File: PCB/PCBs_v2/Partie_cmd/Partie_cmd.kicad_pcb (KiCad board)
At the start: 2 copper layers, 51 parts, among them J2 Conn_01x04_Socket, J3 Conn_01x04_Socket, J4 Conn_01x11_Pin, J5 Conn_01x10_Pin, U1 ESP32-S3-DEVKITC-1-N8R2, U4 XL1509-5.0

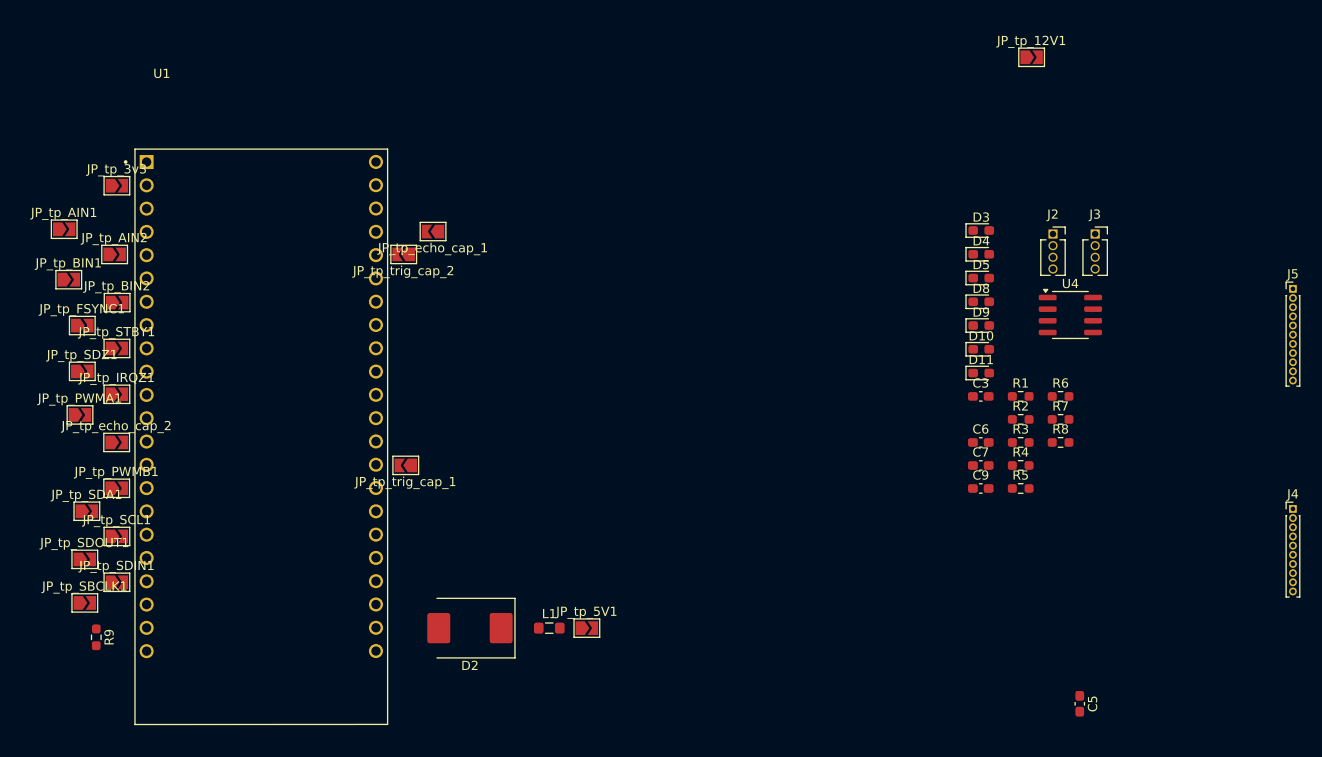
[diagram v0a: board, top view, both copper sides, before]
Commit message: Add new KiCad PCB and schematic files for Partie_cmd
Added new footprints, backup files, and autosave files for the Partie_cmd project in PCBs_v2, including ESP32 and SSOP5 footprints. Updated Partie_cmd.kicad_pcb, Partie_cmd.kicad_sch, and fp-lib-table to reflect new components and changes. Also added autosave and lock files for both PCB_v1 and PCBs_v2 projects.
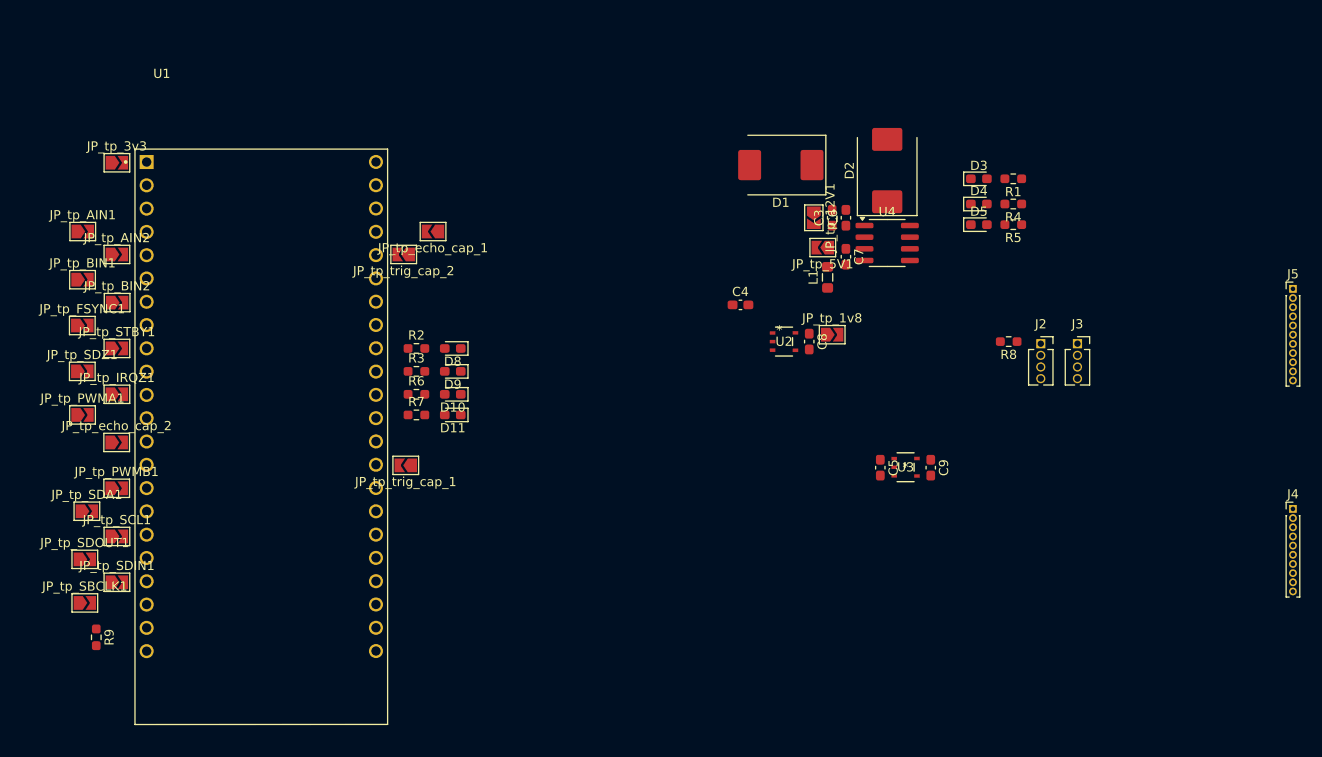
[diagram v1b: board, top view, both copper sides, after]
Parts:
- added C4: 1u, Capacitor_SMD:C_0603_1608Metric_Pad1.08x0.95mm_HandSolder, F.Cu at (127.8, 75.2)
- added C8: 1u, Capacitor_SMD:C_0603_1608Metric_Pad1.08x0.95mm_HandSolder, F.Cu at (135.2, 79.2)
- added D1: MBRS320, Diode_SMD:D_SMC, F.Cu at (132.2, 60.0)
- added JP_tp_1v8: SolderJumper_2_Open, Jumper:SolderJumper-2_P1.3mm_Open_TrianglePad1.0x1.5mm, F.Cu at (137.8, 78.5)
- added U2: BU18SD5WG-TL, footprints:SSOP5_ROM-L, F.Cu at (132.5, 79.2)
- added U3: BU33SD5WG-TR, footprints:SSOP5_ROM-L, F.Cu at (145.8, 93.0)
- moved R7 70.2 mm to (92.4, 87.2)
- moved R6 70.2 mm to (92.4, 85.0)
- moved D2 67.5 mm to (143.8, 60.6), turned to 90 degrees
- moved R3 66.4 mm to (92.4, 82.5)
- moved R2 66.4 mm to (92.4, 80.0)
- moved D8 57.9 mm to (96.4, 80.0), turned to 180 degrees
- moved D9 57.8 mm to (96.4, 82.5), turned to 180 degrees
- moved D10 57.8 mm to (96.4, 85.0), turned to 180 degrees
- moved D11 57.8 mm to (96.4, 87.2), turned to 180 degrees
- moved L1 48.8 mm to (137.2, 72.2), turned to 90 degrees
- moved JP_tp_5V1 48.8 mm to (136.7, 69.0), turned to 180 degrees
- moved C5 33.7 mm to (143.0, 93.0)
- moved JP_tp_12V1 29.5 mm to (135.8, 65.8), turned to -90 degrees
- moved R5 28.8 mm to (157.5, 66.5), turned to 180 degrees
- moved C6 28.6 mm to (139.2, 65.8), turned to 90 degrees
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
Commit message: fin schéma + Routage PCB cmd
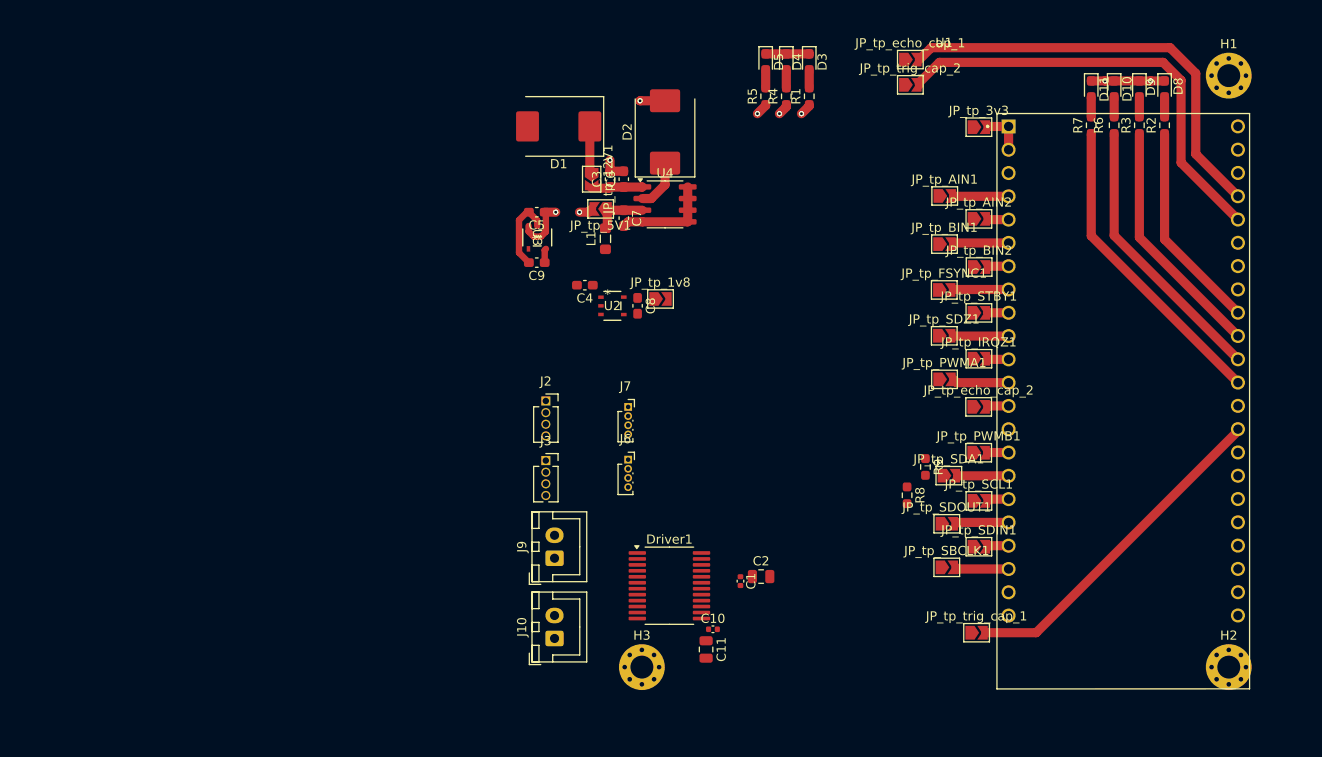
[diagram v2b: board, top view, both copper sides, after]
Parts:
- removed J4: Conn_01x11_Pin, Connector_PinHeader_1.00mm:PinHeader_1x10_P1.00mm_Vertical
- removed J5: Conn_01x10_Pin, Connector_PinHeader_1.00mm:PinHeader_1x11_P1.00mm_Vertical
- added C1: 0.1u, Capacitor_SMD:C_0402_1005Metric, F.Cu at (127.8, 105.4)
- added C10: 0.1u, Capacitor_SMD:C_0402_1005Metric, F.Cu at (124.8, 110.6)
- added C11: 10u, Capacitor_SMD:C_0805_2012Metric, F.Cu at (124.0, 112.8)
- added C2: 10u, Capacitor_SMD:C_0805_2012Metric, F.Cu at (130.0, 104.9)
- added Driver1: TB6612FNG, Package_SO:SSOP-24_5.3x8.2mm_P0.65mm, F.Cu at (120.0, 105.9)
- added H1: MountingHole_Pad, MountingHole:MountingHole_2.5mm_Pad_Via, F.Cu at (181.0, 50.2)
- added H2: MountingHole_Pad, MountingHole:MountingHole_2.5mm_Pad_Via, F.Cu at (181.0, 114.8)
- added H3: MountingHole_Pad, MountingHole:MountingHole_2.5mm_Pad_Via, F.Cu at (117.0, 114.8)
- added J10: Conn_01x02, Connector_JST:JST_XH_B2B-XH-A_1x02_P2.50mm_Vertical, F.Cu at (107.5, 111.6)
- added J6: Conn_01x04, Connector_PinSocket_1.00mm:PinSocket_1x04_P1.00mm_Vertical, F.Cu at (115.5, 92.1)
- added J7: Conn_01x04, Connector_PinSocket_1.00mm:PinSocket_1x04_P1.00mm_Vertical, F.Cu at (115.5, 86.4)
- added J9: Conn_01x02, Connector_JST:JST_XH_B2B-XH-A_1x02_P2.50mm_Vertical, F.Cu at (107.5, 102.9)
- moved JP_tp_3v3 94.1 mm to (153.8, 55.9)
- moved JP_tp_AIN1 94.1 mm to (150.0, 63.4)
- moved JP_tp_AIN2 94.1 mm to (153.8, 65.9)
- moved JP_tp_BIN1 94.1 mm to (150.0, 68.6)
- moved JP_tp_BIN2 94.1 mm to (153.8, 71.1)
- moved JP_tp_FSYNC1 94.1 mm to (150.0, 73.6)
- moved JP_tp_IRQZ1 94.1 mm to (153.8, 81.1)
- moved JP_tp_PWMA1 94.1 mm to (150.0, 83.4)
- moved JP_tp_PWMB1 94.1 mm to (153.7, 91.4)
- moved JP_tp_SBCLK1 94.1 mm to (150.2, 103.9)
- moved JP_tp_SCL1 94.1 mm to (153.8, 96.6)
- moved JP_tp_SDA1 94.1 mm to (150.5, 93.9)
- moved JP_tp_SDIN1 94.1 mm to (153.8, 101.6)
- moved JP_tp_SDOUT1 94.1 mm to (150.2, 99.1)
- moved JP_tp_SDZ1 94.1 mm to (150.0, 78.6)
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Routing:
- net Net-(JP_tp_trig_cap_2-B): track 0.00 -> 48.3 mm
- net Net-(JP_tp_echo_cap_1-B): track 0.00 -> 47.1 mm
- net GND: track 0.00 -> 37.6 mm, vias 0 -> 4
- net Net-(JP_tp_trig_cap_1-B): track 0.00 -> 36.8 mm
- net Net-(U1-GPIO36): track 0.00 -> 33.8 mm
- net Net-(U1-GPIO37): track 0.00 -> 30.2 mm
- net Net-(U1-GPIO38): track 0.00 -> 26.5 mm
- net Net-(U1-MTCK/GPIO39): track 0.00 -> 22.8 mm
- net 5V: track 0.00 -> 7.77 mm, vias 0 -> 2
- net 12V: track 0.00 -> 6.92 mm, vias 0 -> 1
- net Net-(JP_tp_PWMA1-B): track 0.00 -> 6.16 mm
- net 3.3V: track 0.00 -> 6.13 mm, vias 0 -> 1
- net Net-(JP_tp_5V1-A): track 0.00 -> 6.06 mm
- net Net-(JP_tp_BIN1-B): track 0.00 -> 6.06 mm
- net Net-(JP_tp_FSYNC1-B): track 0.00 -> 6.05 mm
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- added copper zone on In2.Cu, net GND
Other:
- copper layers 2 -> 4

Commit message: Routage pcb cmd
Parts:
- added D6: LED_Small, LED_SMD:LED_0603_1608Metric_Pad1.05x0.95mm_HandSolder, F.Cu at (130.4, 48.7)
- added H4: MountingHole_Pad, MountingHole:MountingHole_2.2mm_M2_DIN965_Pad, F.Cu at (116.8, 103.1)
- added H5: MountingHole_Pad, MountingHole:MountingHole_2.2mm_M2_DIN965_Pad, F.Cu at (132.5, 93.7)
- added J1: Barrel_Jack, Connector_BarrelJack:BarrelJack_Wuerth_694108106102_2.5x5.5mm, F.Cu at (113.2, 53.3)
- added J4: Conn_01x13_Pin, Connector_PinHeader_1.27mm:PinHeader_1x13_P1.27mm_Vertical, F.Cu at (131.1, 80.6)
- added JP1: Jumper_2_Bridged, TestPoint:TestPoint_2Pads_Pitch2.54mm_Drill0.8mm, F.Cu at (121.8, 49.8)
- added R10: 1.2k, Resistor_SMD:R_0603_1608Metric_Pad0.98x0.95mm_HandSolder, F.Cu at (130.4, 52.3)
- R4: value 120 -> 1.2k
- R5: value 82 -> 820
- moved JP_tp_3v3 40.7 mm to (117.9, 75.2), turned to -90 degrees
- moved JP_tp_5V1 19.2 mm to (130.3, 71.9), turned to -90 degrees
- moved D1 17.9 mm to (125.2, 60.2)
- moved C3 17.9 mm to (130.8, 65.9)
- moved C6 17.9 mm to (132.3, 65.9)
- moved C7 17.9 mm to (132.3, 70.2)
- moved D2 17.9 mm to (136.8, 60.8)
- moved JP_tp_12V1 17.9 mm to (128.8, 65.9)
- moved U4 17.9 mm to (136.8, 68.7)
- moved L1 16.6 mm to (129.5, 69.4), turned to 0 degrees
- moved C4 15.1 mm to (124.6, 67.0), turned to 90 degrees
- moved C10 14.0 mm to (138.7, 112.0)
- moved C11 14.0 mm to (138.0, 114.2)
- moved Driver1 14.0 mm to (134.0, 107.2)
- moved H3 14.0 mm to (131.0, 116.1)
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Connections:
- C1 pad 1: 5V -> 3.3V
- C2 pad 1: 5V -> 3.3V
- Driver1 pad 20: 5V -> 3.3V
- Driver1 pad 3: (no net) -> GND
- R4 pad 1: 3.3V -> 5V
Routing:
- net 12V: track 6.92 -> 184.8 mm, vias 1 -> 4
- net 5V: track 7.77 -> 168.9 mm, vias 2 -> 5
- net 3.3V: track 6.13 -> 118.0 mm, vias 1 -> 3
- net Echo_cap_1: track 0.00 -> 62.9 mm, vias 0 -> 1
- net Trig_cap_2: track 0.00 -> 61.1 mm
- net BIN2: track 0.00 -> 56.9 mm, vias 0 -> 4
- net SCL: track 0.00 -> 56.3 mm, vias 0 -> 5
- net SDA: track 0.00 -> 55.9 mm, vias 0 -> 4
- net BIN1: track 0.00 -> 51.2 mm, vias 0 -> 2
- net AIN1: track 0.00 -> 50.3 mm, vias 0 -> 2
- net AIN2: track 0.00 -> 49.1 mm, vias 0 -> 2
- net GND: track 37.6 -> 86.3 mm, vias 4 -> 14
- net Trig_cap_1: track 0.00 -> 43.6 mm, vias 0 -> 1
- net STBY: track 0.00 -> 41.0 mm, vias 0 -> 4
- net 1.8V: track 1.36 -> 41.7 mm, vias 1 -> 2
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- added copper zone on In1.Cu, net 1.8V
- added copper zone on In1.Cu, net 12V
- added copper zone on In1.Cu, net 3.3V
- added copper zone on In1.Cu, net 5V
- added copper zone on B.Cu, net GND
- added copper zone on F.Cu, net GND
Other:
- board outline added: 79.2 x 75 mm
- board text added: "G-Vidon S-Remy A-Djokic A-Taillepierre J-Lepetit C-Laroche"
- board text added: "NOMAD_"

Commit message: Fin routage pcb cmd
:(
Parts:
- removed J7: Conn_01x04, Connector_PinSocket_1.00mm:PinSocket_1x04_P1.00mm_Vertical
- J4: value Conn_01x13_Pin -> Conn_01x12; footprint Connector_PinHeader_1.27mm:PinHeader_1x13_P1.27mm_Vertical -> Connector_PinHeader_1.27mm:PinHeader_1x12_P1.27mm_Vertical
- moved J3 30.3 mm to (111.2, 61.8)
- moved J2 17.7 mm to (111.2, 68.3)
- moved J6 14.7 mm to (136.8, 82.2)
- moved H5 5.17 mm to (130.0, 98.2)
- moved H4 4.86 mm to (117.2, 98.2)
- moved J9 3.22 mm to (121.2, 107.5)
- moved J10 2.92 mm to (121.2, 115.9)
- moved J4 1.07 mm to (130.0, 80.8)
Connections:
- J4 pad 1: FSYNC -> SDZ
- J4 pad 11: 12V -> GND
- J4 pad 12: GND -> 12V
- J4 pad 2: SBCLK -> IRQZ
- J4 pad 3: SDIN -> 1.8V
- J4 pad 4: SCL -> SDA
- J4 pad 5: SDA -> SCL
- J4 pad 6: SDZ -> SBCLK
- J4 pad 7: IRQZ -> FSYNC
- J4 pad 8: SDOUT -> SDIN
- J4 pad 9: 1.8V -> SDOUT
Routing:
- net 5V: track 168.9 -> 233.8 mm, vias 5 -> 7
- net Trig_cap_1: track 43.6 -> 85.9 mm
- net 12V: track 184.8 -> 143.9 mm
- net SDA: track 55.9 -> 31.6 mm, vias 4 -> 2
- net SCL: track 56.3 -> 33.1 mm, vias 5 -> 2
- net Echo_cap_1: track 62.9 -> 40.9 mm
- net Trig_cap_2: track 61.1 -> 42.0 mm, vias 0 -> 1
- net Echo_cap_2: track 38.7 -> 52.8 mm
- net SDIN: track 33.9 -> 44.4 mm
- net SBCLK: track 31.5 -> 40.2 mm
- net GND: track 86.3 -> 93.3 mm, vias 14 -> 15
- net SDZ: track 26.4 -> 20.1 mm
- net IRQZ: track 32.3 -> 26.3 mm
- net FSYNC: track 24.2 -> 29.8 mm, vias 2 -> 0
- net 1.8V: track 41.7 -> 47.2 mm
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- added copper zone on In1.Cu, net GND

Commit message: fin routage pcb 1.1
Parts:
- added J7: Conn_01x04, Connector_PinHeader_1.27mm:PinHeader_1x04_P1.27mm_Vertical, F.Cu at (132.8, 88.0)
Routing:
- net SCL: track 33.1 -> 48.6 mm
- net GND: track 93.3 -> 105.5 mm, vias 15 -> 31
- net 5V: track 233.8 -> 242.9 mm
- net SDA: track 31.6 -> 40.5 mm
- net 12V: track 143.9 -> 147.6 mm

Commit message: Fin routage 1.2
pour de vrai cette foix?
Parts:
- moved J7 0.42 mm to (133.2, 88.0)
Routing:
- net 5V: track 242.9 -> 240.6 mm
- net SCL: track 48.6 -> 50.2 mm

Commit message: replacement trous de perçage
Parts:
- moved H1 65.1 mm to (181.0, 115.3)
- moved H2 64.4 mm to (181.0, 50.3)
- moved H3 0.20 mm to (131.1, 116.0)
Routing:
- net GND: track 105.5 -> 104.8 mm

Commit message: fin du routage
svpsvpsvpsvpsvp
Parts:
- removed J4: Conn_01x12, Connector_PinHeader_1.27mm:PinHeader_1x12_P1.27mm_Vertical
- added J5: Conn_01x14, Connector_PinHeader_1.27mm:PinHeader_1x14_P1.27mm_Vertical, F.Cu at (132.6, 80.7)
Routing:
- net 12V: track 147.6 -> 158.2 mm
- net IRQZ: track 26.3 -> 23.5 mm
- net SDZ: track 20.1 -> 17.5 mm
- net 5V: track 240.6 -> 238.3 mm
- net 1.8V: track 47.2 -> 49.5 mm
- net SDA: track 40.7 -> 38.5 mm
- net FSYNC: track 29.8 -> 28.1 mm
- net GND: track 104.8 -> 106.4 mm
- net SBCLK: track 40.2 -> 39.2 mm
- net SDIN: track 44.4 -> 43.4 mm
- net SCL: track 50.2 -> 49.2 mm
- net SDOUT: track 40.4 -> 39.4 mm
